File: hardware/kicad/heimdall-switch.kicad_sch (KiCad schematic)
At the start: 42 parts, among them J1 TC2030-NL (SWD), J2 LOAD_OUT, J3 BATT_IN, J4 B3B-XH-A, Q1 AO3400A, Q2 BSS84, Q3 AO4407A, Q4 AO4407A, Q5 AO3400A, Q6 BSS84, SW1 PTS810, U1 BT832, U2 TPS629206, Y1 32.768kHz

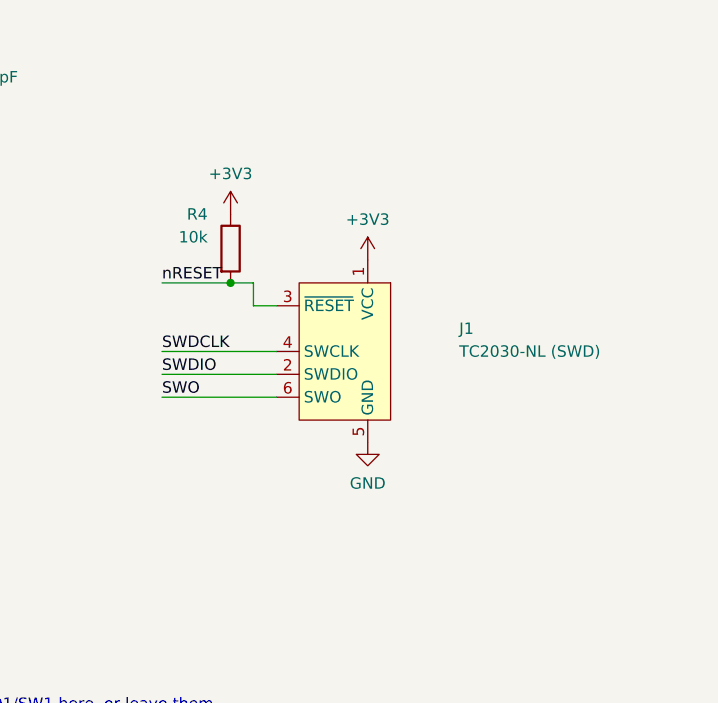
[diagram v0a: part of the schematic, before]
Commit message: Revert "J1: Tag-Connect TC2030-NL in place of the 2x5 SWD header"
This reverts commit dd4bac91d17cbcc49fd8600aaa5e4591b524028c.
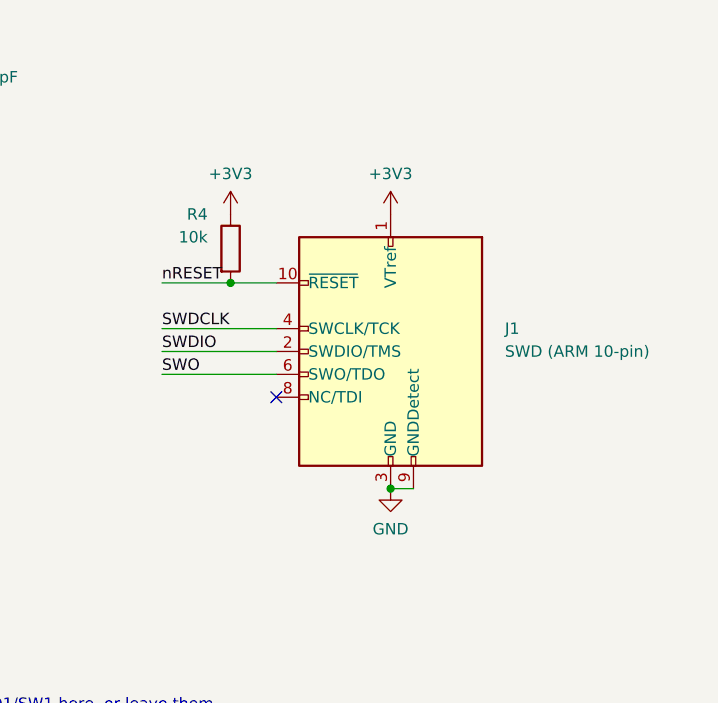
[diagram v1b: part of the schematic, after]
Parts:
- J1: value TC2030-NL (SWD) -> SWD (ARM 10-pin); footprint Connector:Tag-Connect_TC2030-IDC-NL_2x03_P1.27mm_Vertical -> Connector_PinHeader_1.27mm:PinHeader_2x05_P1.27mm_Vertical_SMD; symbol Connector:Conn_ARM_SWD_TagConnect_TC2030-NL -> Connector:Conn_ARM_JTAG_SWD_10; LCSC (none) -> C5155080; now in the parts list
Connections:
- net GND: now also J1.3 (GND), J1.9 (GNDDetect)
- net nRESET: now also J1.10 (~{RESET}); no longer J1.3 (~{RESET})
- no-connect marks 6 -> 7
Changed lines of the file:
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@@
 	)
 	(junction
+		(at 292.1 127)
+		(diameter 0)
+		(color 0 0 0 0)
+	)
+	(junction
 		(at 71.12 48.26)
 		(diameter 0)
@@
 	)
 	(no_connect
+		(at 279.4 116.84)
+	)
+	(no_connect
 		(at 195.58 71.12)
 	)
@@
 	(wire
 		(pts
+			(xy 294.64 127) (xy 292.1 127)
+		)
+		(stroke
+			(width 0)
+			(type default)
+		)
+	)
+	(wire
+		(pts
 			(xy 27.94 167.64) (xy 34.29 167.64)
 		)
@@
 	(wire
 		(pts
-			(xy 266.7 111.76) (xy 279.4 111.76)
+			(xy 266.7 109.22) (xy 279.4 109.22)
 		)
 		(stroke
@@
 	(wire
 		(pts
-			(xy 266.7 114.3) (xy 279.4 114.3)
+			(xy 266.7 111.76) (xy 279.4 111.76)
 		)
 		(stroke
@@
 	(wire
 		(pts
-			(xy 274.32 104.14) (xy 276.86 104.14)
-		)
-		(stroke
-			(width 0)
-			(type default)
-		)
-	)
-	(wire
-		(pts
-			(xy 276.86 104.14) (xy 276.86 106.68)
-		)
-		(stroke
-			(width 0)
-			(type default)
-		)
-	)
-	(wire
-		(pts
-			(xy 276.86 106.68) (xy 279.4 106.68)
+			(xy 274.32 104.14) (xy 279.4 104.14)
 		)
 		(stroke
@@
 	(wire
 		(pts
-			(xy 266.7 116.84) (xy 279.4 116.84)
+			(xy 266.7 114.3) (xy 279.4 114.3)
 		)
 		(stroke
@@
 	)
 	(label "SWO"
-		(at 266.7 116.84 0)
+		(at 266.7 114.3 0)
 		(effects
 			(font
@@
 	)
 	(label "SWDIO"
-		(at 266.7 114.3 0)
+		(at 266.7 111.76 0)
 		(effects
 			(font
@@
 	)
 	(label "SWDCLK"
-		(at 266.7 111.76 0)
+		(at 266.7 109.22 0)
 		(effects
 			(font
@@
 	(symbol
 		(lib_id "power:GND")
-		(at 289.56 121.92 0)
+		(at 292.1 127 0)
 		(unit 1)
 		(body_style 1)
@@
 		(dnp no)
 		(property "Reference" "#PWR112"
-			(at 289.56 121.92 0)
+			(at 292.1 127 0)
 			(hide yes)
 			(show_name no)
@@
 		)
 		(property "Value" "GND"
-			(at 289.56 126.42 0)
+			(at 292.1 131.5 0)
 			(show_name no)
 			(do_not_autoplace no)
@@
 		)
 		(property "Footprint" ""
-			(at 289.56 121.92 0)
+			(at 292.1 127 0)
 			(hide yes)
 			(show_name no)
@@
 		)
 		(property "Datasheet" ""
-			(at 289.56 121.92 0)
+			(at 292.1 127 0)
 			(hide yes)
 			(show_name no)
@@
 		)
 		(property "Description" ""
-			(at 289.56 121.92 0)
+			(at 292.1 127 0)
 			(show_name no)
 			(do_not_autoplace no)
@@
 	(symbol
 		(lib_id "power:+3V3")
-		(at 289.56 101.6 0)
+		(at 292.1 96.52 0)
 		(unit 1)
 		(body_style 1)
@@
 		(dnp no)
 		(property "Reference" "#PWR111"
-			(at 289.56 101.6 0)
+			(at 292.1 96.52 0)
 			(hide yes)
 			(show_name no)
@@
 		)
 		(property "Value" "+3V3"
-			(at 289.56 97.1 0)
+			(at 292.1 92.02 0)
 			(show_name no)
 			(do_not_autoplace no)
@@
 		)
 		(property "Footprint" ""
-			(at 289.56 101.6 0)
+			(at 292.1 96.52 0)
 			(hide yes)
 			(show_name no)
@@
 		)
 		(property "Datasheet" ""
-			(at 289.56 101.6 0)
+			(at 292.1 96.52 0)
 			(hide yes)
 			(show_name no)
@@
 		)
 		(property "Description" ""
-			(at 289.56 101.6 0)
+			(at 292.1 96.52 0)
 			(show_name no)
 			(do_not_autoplace no)
@@
 	)
 	(symbol
-		(lib_id "Connector:Conn_ARM_SWD_TagConnect_TC2030-NL")
-		(at 287.02 111.76 0)
+		(lib_id "Connector:Conn_ARM_JTAG_SWD_10")
+		(at 292.1 111.76 0)
 		(mirror y)
 		(unit 1)
 		(body_style 1)
 		(exclude_from_sim no)
-		(in_bom no)
+		(in_bom yes)
 		(on_board yes)
 		(in_pos_files yes)
 		(dnp no)
 		(property "Reference" "J1"
-			(at 299.72 109.22 0)
+			(at 304.8 109.22 0)
 			(show_name no)
 			(do_not_autoplace no)
@@
 			)
 		)
-		(property "Value" "TC2030-NL (SWD)"
-			(at 299.72 111.76 0)
+		(property "Value" "SWD (ARM 10-pin)"
+			(at 304.8 111.76 0)
 			(show_name no)
 			(do_not_autoplace no)
@@
 			)
 		)
-		(property "Footprint" "Connector:Tag-Connect_TC2030-IDC-NL_2x03_P1.27mm_Vertical"
-			(at 287.02 111.76 0)
+		(property "Footprint" "Connector_PinHeader_1.27mm:PinHeader_2x05_P1.27mm_Vertical_SMD"
+			(at 292.1 111.76 0)
 			(hide yes)
 			(show_name no)
@@
 			)
 		)
-		(property "Datasheet" "https://www.tag-connect.com/wp-content/uploads/bsk-pdf-manager/TC2030-CTX_1.pdf"
-			(at 287.02 111.76 0)
+		(property "Datasheet" ""
+			(at 292.1 111.76 0)
 			(hide yes)
 			(show_name no)
@@
 		)
 		(property "Description" ""
-			(at 287.02 111.76 0)
+			(at 292.1 111.76 0)
 			(show_name no)
 			(do_not_autoplace no)
@@
 			)
 		)
-		(property "LCSC" ""
-			(at 287.02 111.76 0)
+		(property "LCSC" "C5155080"
+			(at 292.1 111.76 0)
 			(hide yes)
 			(show_name no)
@@
 		(pin "6"
 		)
+		(pin "7"
+		)
+		(pin "8"
+		)
+		(pin "9"
+		)
+		(pin "10"
+		)
 		(instances
